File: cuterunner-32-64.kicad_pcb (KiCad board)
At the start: 2 copper layers, 48 parts, among them J1 Conn_01x05, J2 Conn_02x06_Row_Letter_Last, J3 Conn_Coaxial, J4 Conn_01x03, J5 Conn_Coaxial, J6 Conn_01x03, SW1 SW_Push_Dual, SW2 SW_Push_Dual, SW3 SW_Push_Dual, SW4 SW_Push_Dual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

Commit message: Placement of components
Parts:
- added R15: 22, Resistor_SMD:R_0805_2012Metric_Pad1.15x1.40mm_HandSolder, F.Cu at (124.7, 113.0)
- J2: value Conn_02x06_Row_Letter_Last -> Conn_02x06_Odd_Even
- moved R7 59.7 mm to (153.9, 133.3), turned to 180 degrees
- moved J2 57.2 mm to (152.4, 109.2)
- moved D3 51.3 mm to (158.5, 133.3), turned to 180 degrees
- moved R14 37.0 mm to (153.9, 146.1), turned to 180 degrees
- moved R5 35.9 mm to (153.9, 128.3), turned to 180 degrees
- moved D8 34.6 mm to (158.5, 146.1), turned to 180 degrees
- moved TP1 32.1 mm to (119.4, 116.8)
- moved D1 30.4 mm to (158.5, 128.3), turned to 180 degrees
- moved R12 30.1 mm to (153.9, 141.0), turned to 180 degrees
- moved D4 28.3 mm to (158.5, 135.9), turned to 180 degrees
- moved R8 26.0 mm to (153.9, 135.9), turned to 180 degrees
- moved R13 25.3 mm to (153.9, 143.5), turned to 180 degrees
- moved J5 24.4 mm to (143.5, 108.0)
- moved J6 24.4 mm to (141.0, 114.3)
- moved D7 24.2 mm to (158.5, 143.5), turned to 180 degrees
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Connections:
- J2 pad 1: (no net) -> /PMOD0
- J2 pad 10: (no net) -> GND
- J2 pad 11: (no net) -> +3V3
- J2 pad 12: (no net) -> +3V3
- J2 pad 2: (no net) -> /PMOD4
- J2 pad 3: (no net) -> /PMOD1
- J2 pad 4: (no net) -> /PMOD5
- J2 pad 5: (no net) -> /PMOD2
- J2 pad 6: (no net) -> /PMOD6
- J2 pad 7: (no net) -> /PMOD3
- J2 pad 8: (no net) -> /PMOD7
- J2 pad 9: (no net) -> GND
- U5 pad 3: /CLK0 -> Net-(R15-Pad2)
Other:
- board outline added: 76.2 x 50.8 mm
- net class Default: clearance 0.2 -> 0.2032; trace_width 0.25 -> 0.2032; via_dia 0.8 -> 0.635; via_drill 0.4 -> 0.3048
- rule trace_clearance: 0.2 -> 0.2032
- rule trace_min: 0.2 -> 0.2032
- rule via_min_drill: 0.3 -> 0.3048
- rule via_min_size: 0.4 -> 0.635

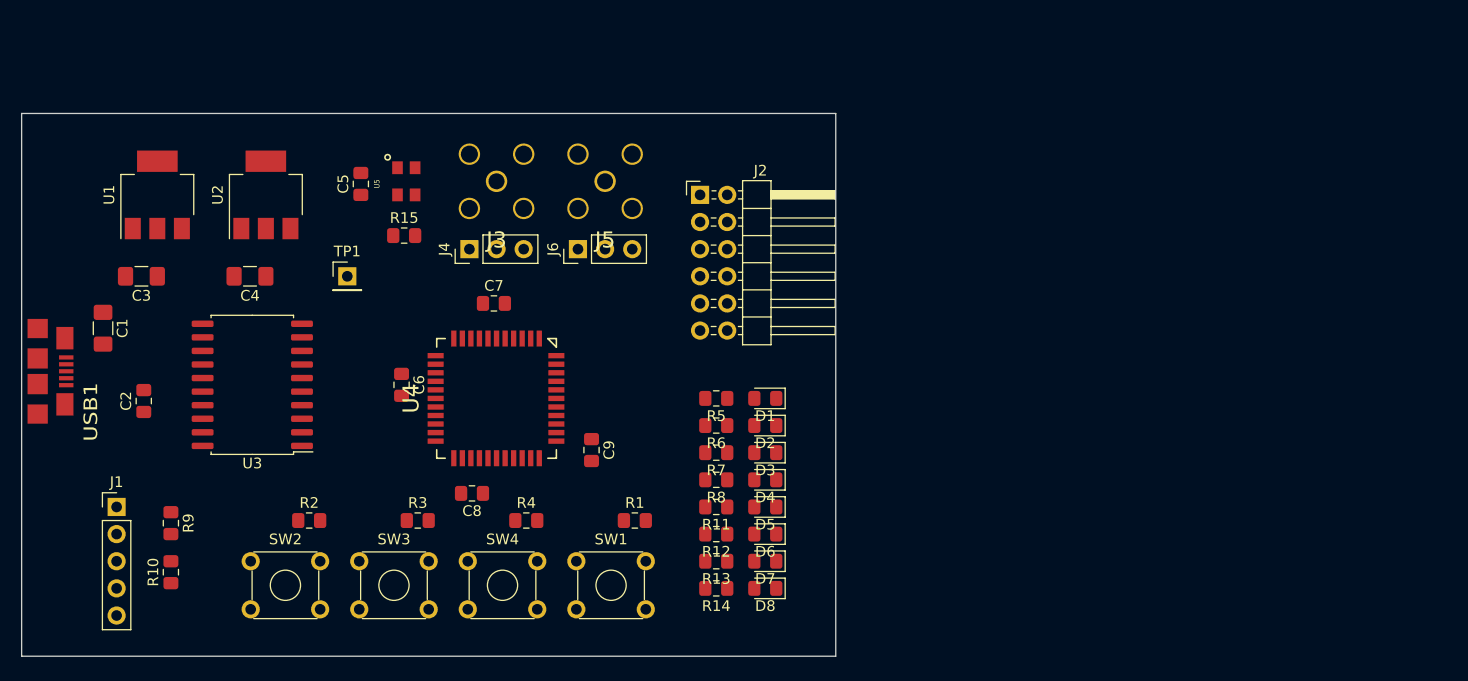
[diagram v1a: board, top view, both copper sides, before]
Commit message: Very sloppy first pass routing
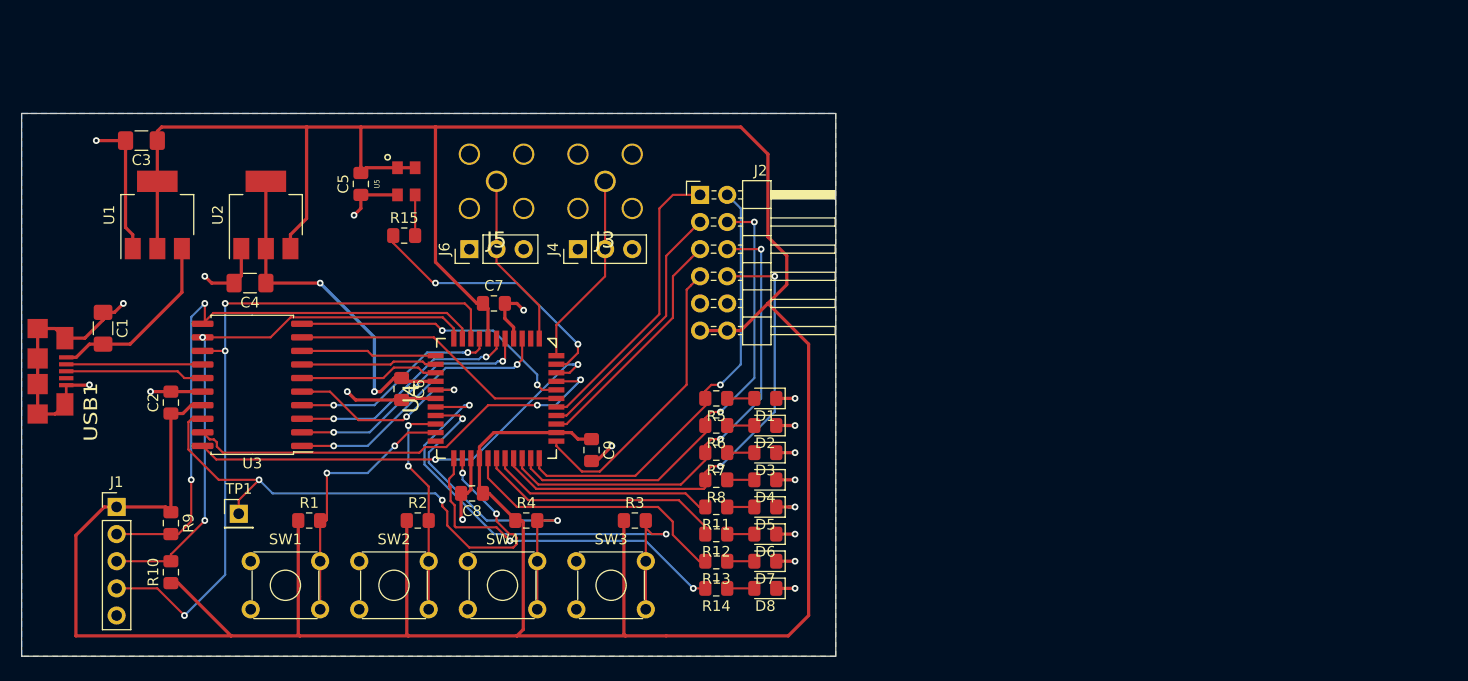
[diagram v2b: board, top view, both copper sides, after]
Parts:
- moved R1 30.5 mm to (115.8, 139.7)
- moved SW1 30.5 mm to (110.3, 143.5)
- moved TP1 24.4 mm to (109.2, 139.1)
- moved R3 20.3 mm to (146.3, 139.7)
- moved SW3 20.3 mm to (140.8, 143.5)
- moved C3 12.7 mm to (100.1, 104.1)
- moved J3 10.2 mm to (143.5, 108.0)
- moved J4 10.2 mm to (141.0, 114.3)
- moved J5 10.2 mm to (133.3, 108.0)
- moved J6 10.2 mm to (130.8, 114.3)
- moved R2 10.2 mm to (126.0, 139.7)
- moved SW2 10.2 mm to (120.5, 143.5)
- moved C2 2.54 mm to (102.9, 128.7)
- moved U1 1.88 mm to (101.6, 111.1)
- moved U2 1.88 mm to (111.8, 111.1)
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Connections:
- U4 pad 12: /IFACE4 -> /IFACE7
- U4 pad 13: /IFACE5 -> /IFACE6
- U4 pad 14: /IFACE6 -> /IFACE5
- U4 pad 16: /IFACE7 -> /IFACE4
- USB1 pad 5: Net-(USB1-Pad5) -> GND
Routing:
- net +3V3: track 0.00 -> 340.1 mm
- net GND: track 0.00 -> 93.3 mm, vias 0 -> 18
- net /TDI_SWDIO: track 0.00 -> 66.3 mm, vias 0 -> 3
- net /TMS_~RST: track 0.00 -> 56.7 mm, vias 0 -> 2
- net /TDO: track 0.00 -> 54.1 mm, vias 0 -> 4
- net /TCK_SWCLK: track 0.00 -> 53.1 mm, vias 0 -> 2
- net /BUT3: track 0.00 -> 47.2 mm, vias 0 -> 2
- net /PMOD7: track 0.00 -> 47.0 mm, vias 0 -> 2
- net /PMOD6: track 0.00 -> 45.2 mm, vias 0 -> 2
- net /PMOD5: track 0.00 -> 44.3 mm, vias 0 -> 2
- net /IFACE_CTRL2: track 0.00 -> 42.0 mm, vias 0 -> 2
- net /IFACE_CTRL3: track 0.00 -> 41.7 mm, vias 0 -> 2
- net /PMOD4: track 0.00 -> 41.6 mm, vias 0 -> 1
- net +1V8: track 0.00 -> 33.3 mm, vias 0 -> 2
- net /LED7: track 0.00 -> 32.7 mm, vias 0 -> 2
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- added copper zone on B.Cu, net GND
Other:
- net class Power added: clearance 0.3048, trace_width 0.3048, via_dia 0.635, via_drill 0.3048
- rule pad_to_mask_clearance: 0.051 -> 0.0508

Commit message: Good enough trace routing to ship
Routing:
- net +3V3: track 340.1 -> 362.3 mm
- net GND: track 93.3 -> 77.2 mm, vias 18 -> 19
- net /PMOD0: track 27.5 -> 31.6 mm
- net /PMOD1: track 24.2 -> 28.3 mm
- net /TDO: track 54.1 -> 50.2 mm
- net /PMOD2: track 22.5 -> 26.4 mm
- net +1V8: track 33.3 -> 30.7 mm
- net /BUT3: track 47.2 -> 45.6 mm
- net /PMOD3: track 27.7 -> 28.7 mm
- net /CLK0: track 25.2 -> 26.2 mm
- net /TCK_SWCLK: track 53.1 -> 54.1 mm
- net /TDI_SWDIO: track 66.3 -> 65.6 mm

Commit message: Ship it
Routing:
- net +3V3: track 362.3 -> 361.8 mm
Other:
- board text added: "2019-12-17"
- board text added: "CuteRunner Rev A XC2C32A/XC2C64A Dev Board "Just in time for 36C3" Edition"
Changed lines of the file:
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@@
   (general
     (thickness 1.6)
-    (drawings 4)
-    (tracks 505)
+    (drawings 6)
+    (tracks 506)
     (zones 0)
     (modules 49)
@@
     (47 F.CrtYd user)
     (48 B.Fab user)
-    (49 F.Fab user hide)
+    (49 F.Fab user)
   )
   (setup
@@
     (solder_mask_margin 0.05)
     (solder_paste_ratio -0.1)
-    (fp_text reference U5 (at 0.25 2.75 90) (layer F.SilkS)
-      (effects (font (size 0.508 0.457) (thickness 0.11425)))
+    (fp_text reference U5 (at -3.429 -0.063 180) (layer F.SilkS)
+      (effects (font (size 1.016 1.016) (thickness 0.11425)))
     )
     (fp_text value "50 MHz" (at 0.25 3.5 90) (layer F.SilkS) hide
@@
   (module azonenberg:QFP_44_0.8MM (layer F.Cu)
     (at 133.35 128.27 270)
-    (fp_text reference U4 (at 0 8 90) (layer F.SilkS)
+    (fp_text reference U4 (at 7.366 6.477 180) (layer F.SilkS)
       (effects (font (size 1.5 1.5) (thickness 0.15)))
     )
@@
     (tags "resistor handsolder")
     (attr smd)
-    (fp_text reference R14 (at 0 -1.65) (layer F.SilkS)
+    (fp_text reference R14 (at 3.547 0) (layer F.SilkS)
       (effects (font (size 1 1) (thickness 0.15)))
     )
@@
     (tags "resistor handsolder")
     (attr smd)
-    (fp_text reference R13 (at 0 -1.65) (layer F.SilkS)
+    (fp_text reference R13 (at 3.547 0) (layer F.SilkS)
       (effects (font (size 1 1) (thickness 0.15)))
     )
@@
     (tags "resistor handsolder")
     (attr smd)
-    (fp_text reference R12 (at 0 -1.65) (layer F.SilkS)
+    (fp_text reference R12 (at 3.547 0) (layer F.SilkS)
       (effects (font (size 1 1) (thickness 0.15)))
     )
@@
     (tags "resistor handsolder")
     (attr smd)
-    (fp_text reference R11 (at 0 -1.65) (layer F.SilkS)
+    (fp_text reference R11 (at 3.547 0) (layer F.SilkS)
       (effects (font (size 1 1) (thickness 0.15)))
     )
@@
     (tags "resistor handsolder")
     (attr smd)
-    (fp_text reference R8 (at 0 -1.65) (layer F.SilkS)
+    (fp_text reference R8 (at 3.547 -0.127) (layer F.SilkS)
       (effects (font (size 1 1) (thickness 0.15)))
     )
@@
     (tags "resistor handsolder")
     (attr smd)
-    (fp_text reference R7 (at 0 -1.65) (layer F.SilkS)
+    (fp_text reference R7 (at 3.547 0) (layer F.SilkS)
       (effects (font (size 1 1) (thickness 0.15)))
     )
@@
     (tags "resistor handsolder")
     (attr smd)
-    (fp_text reference R6 (at 0 -1.65) (layer F.SilkS)
+    (fp_text reference R6 (at 3.547 0) (layer F.SilkS)
       (effects (font (size 1 1) (thickness 0.15)))
     )
@@
     (tags "resistor handsolder")
     (attr smd)
-    (fp_text reference R5 (at 0 -1.65) (layer F.SilkS)
+    (fp_text reference R5 (at 3.547 0) (layer F.SilkS)
       (effects (font (size 1 1) (thickness 0.15)))
     )
@@
     (tags "LED handsolder")
     (attr smd)
-    (fp_text reference D8 (at 0 -1.65) (layer F.SilkS)
+    (fp_text reference D8 (at -4.436 0) (layer F.SilkS)
       (effects (font (size 1 1) (thickness 0.15)))
     )
@@
     (tags "LED handsolder")
     (attr smd)
-    (fp_text reference D7 (at 0 -1.65) (layer F.SilkS)
+    (fp_text reference D7 (at -4.436 0) (layer F.SilkS)
       (effects (font (size 1 1) (thickness 0.15)))
     )
@@
     (tags "LED handsolder")
     (attr smd)
-    (fp_text reference D6 (at 0 -1.65) (layer F.SilkS)
+    (fp_text reference D6 (at -4.436 0) (layer F.SilkS)
       (effects (font (size 1 1) (thickness 0.15)))
     )
@@
     (tags "LED handsolder")
     (attr smd)
-    (fp_text reference D5 (at 0 -1.65) (layer F.SilkS)
+    (fp_text reference D5 (at -4.436 0) (layer F.SilkS)
       (effects (font (size 1 1) (thickness 0.15)))
     )
@@
     (tags "LED handsolder")
     (attr smd)
-    (fp_text reference D4 (at 0 -1.65) (layer F.SilkS)
+    (fp_text reference D4 (at -4.436 0) (layer F.SilkS)
       (effects (font (size 1 1) (thickness 0.15)))
     )
@@
     (tags "LED handsolder")
     (attr smd)
-    (fp_text reference D3 (at 0 -1.65) (layer F.SilkS)
+    (fp_text reference D3 (at -4.436 0) (layer F.SilkS)
       (effects (font (size 1 1) (thickness 0.15)))
     )
@@
     (tags "LED handsolder")
     (attr smd)
-    (fp_text reference D2 (at 0 -1.65) (layer F.SilkS)
+    (fp_text reference D2 (at -4.436 0) (layer F.SilkS)
       (effects (font (size 1 1) (thickness 0.15)))
     )
@@
     (tags "LED handsolder")
     (attr smd)
-    (fp_text reference D1 (at 0 -1.65) (layer F.SilkS)
+    (fp_text reference D1 (at -4.436 0) (layer F.SilkS)
       (effects (font (size 1 1) (thickness 0.15)))
     )
@@
       (rotate (xyz 0 0 0))
     )
+  )
+  (gr_text "CuteRunner Rev A\nXC2C32A/XC2C64A Dev Board\n\"Just in time for 36C3\" Edition" (at 116.713 107.061) (layer B.SilkS)
+    (effects (font (size 1.016 1.016) (thickness 0.254)) (justify left mirror))
+  )
+  (gr_text 2019-12-17 (at 160.528 102.87) (layer B.Cu)
+    (effects (font (size 0.762 0.762) (thickness 0.1905)) (justify mirror))
   )
   (gr_line (start 165.1 152.4) (end 88.9 152.4) (layer Edge.Cuts) (width 0.05))
@@
   (segment (start 145.288 151.638) (end 145.288 150.368) (width 0.3048) (layer F.Cu) (net 3))
   (segment (start 145.288 150.368) (end 145.27 150.35) (width 0.3048) (layer F.Cu) (net 3))
-  (segment (start 120.65 102.362) (end 161.163 102.362) (width 0.3048) (layer F.Cu) (net 3))
-  (segment (start 161.544 151.638) (end 125.73 151.638) (width 0.3048) (layer F.Cu) (net 3))
-  (segment (start 161.163 102.362) (end 164.338 105.537) (width 0.3048) (layer F.Cu) (net 3))
-  (segment (start 164.338 105.537) (end 164.338 148.844) (width 0.3048) (layer F.Cu) (net 3))
-  (segment (start 164.338 148.844) (end 161.544 151.638) (width 0.3048) (layer F.Cu) (net 3))
   (segment (start 124.95 150.35) (end 124.95 139.7) (width 0.3048) (layer F.Cu) (net 3))
   (segment (start 125.73 151.638) (end 124.95 151.638) (width 0.3048) (layer F.Cu) (net 3))
@@
   (segment (start 105.84 128.905) (end 104.521 128.905) (width 0.3048) (layer F.Cu) (net 3))
   (segment (start 104.521 128.905) (end 103.741 129.685) (width 0.3048) (layer F.Cu) (net 3))
+  (segment (start 161.544 151.638) (end 125.73 151.638) (width 0.3048) (layer F.Cu) (net 3))
+  (segment (start 164.338 148.844) (end 161.544 151.638) (width 0.3048) (layer F.Cu) (net 3))
+  (segment (start 153.797 102.362) (end 155.956 104.521) (width 0.3048) (layer F.Cu) (net 3))
+  (segment (start 155.956 104.521) (end 162.433 104.521) (width 0.3048) (layer F.Cu) (net 3))
+  (segment (start 120.65 102.362) (end 153.797 102.362) (width 0.3048) (layer F.Cu) (net 3))
+  (segment (start 162.433 104.521) (end 164.338 106.426) (width 0.3048) (layer F.Cu) (net 3))
+  (segment (start 164.338 106.426) (end 164.338 148.844) (width 0.3048) (layer F.Cu) (net 3))
   (segment (start 111.76 114.25) (end 111.76 117.475) (width 0.3048) (layer F.Cu) (net 4))
   (segment (start 124.765 126.67) (end 124.46 126.365) (width 0.3048) (layer F.Cu) (net 4))
@@
   (segment (start 150.368 139.319) (end 150.368 141.351) (width 0.2032) (layer F.Cu) (net 28))
   (segment (start 149.479 138.43) (end 150.368 139.319) (width 0.2032) (layer F.Cu) (net 28))
-  (via (at 151.765 146.05) (size 0.635) (drill 0.3048) (layers F.Cu B.Cu) (net 29))
-  (segment (start 151.765 146.05) (end 152.89 146.05) (width 0.2032) (layer F.Cu) (net 29))
   (segment (start 129.35 134.8232) (end 128.8968 135.2764) (width 0.2032) (layer F.Cu) (net 29))
   (segment (start 128.8968 135.2764) (end 128.8968 139.6918) (width 0.2032) (layer F.Cu) (net 29))
@@
   (segment (start 130.487988 140.462) (end 130.937 140.462) (width 0.2032) (layer F.Cu) (net 29))
   (segment (start 129.667 140.462) (end 130.487988 140.462) (width 0.2032) (layer F.Cu) (net 29))
-  (segment (start 136.525 146.05) (end 131.254499 140.779499) (width 0.2032) (layer B.Cu) (net 29))
   (via (at 130.937 140.462) (size 0.635) (drill 0.3048) (layers F.Cu B.Cu) (net 29))
-  (segment (start 131.254499 140.779499) (end 130.937 140.462) (width 0.2032) (layer B.Cu) (net 29))
-  (segment (start 151.765 146.05) (end 136.525 146.05) (width 0.2032) (layer B.Cu) (net 29))
   (segment (start 129.35 133.87) (end 129.35 134.8232) (width 0.2032) (layer F.Cu) (net 29))
+  (via (at 148.335998 146.05) (size 0.635) (drill 0.3048) (layers F.Cu B.Cu) (net 29))
+  (segment (start 152.89 146.05) (end 148.335998 146.05) (width 0.2032) (layer F.Cu) (net 29))
+  (segment (start 136.525 146.05) (end 148.335998 146.05) (width 0.2032) (layer B.Cu) (net 29))
+  (segment (start 130.937 140.462) (end 136.525 146.05) (width 0.2032) (layer B.Cu) (net 29))
   (via (at 133.35 139.065) (size 0.635) (drill 0.3048) (layers F.Cu B.Cu) (net 30))
   (via (at 128.27 137.795) (size 0.635) (drill 0.3048) (layers F.Cu B.Cu) (net 30))
